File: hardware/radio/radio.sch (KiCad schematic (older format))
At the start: 4 parts, among them P101 CONN_01X04, P102 CONN_02X03, P103 CONN_02X05, P104 CONN_01X02

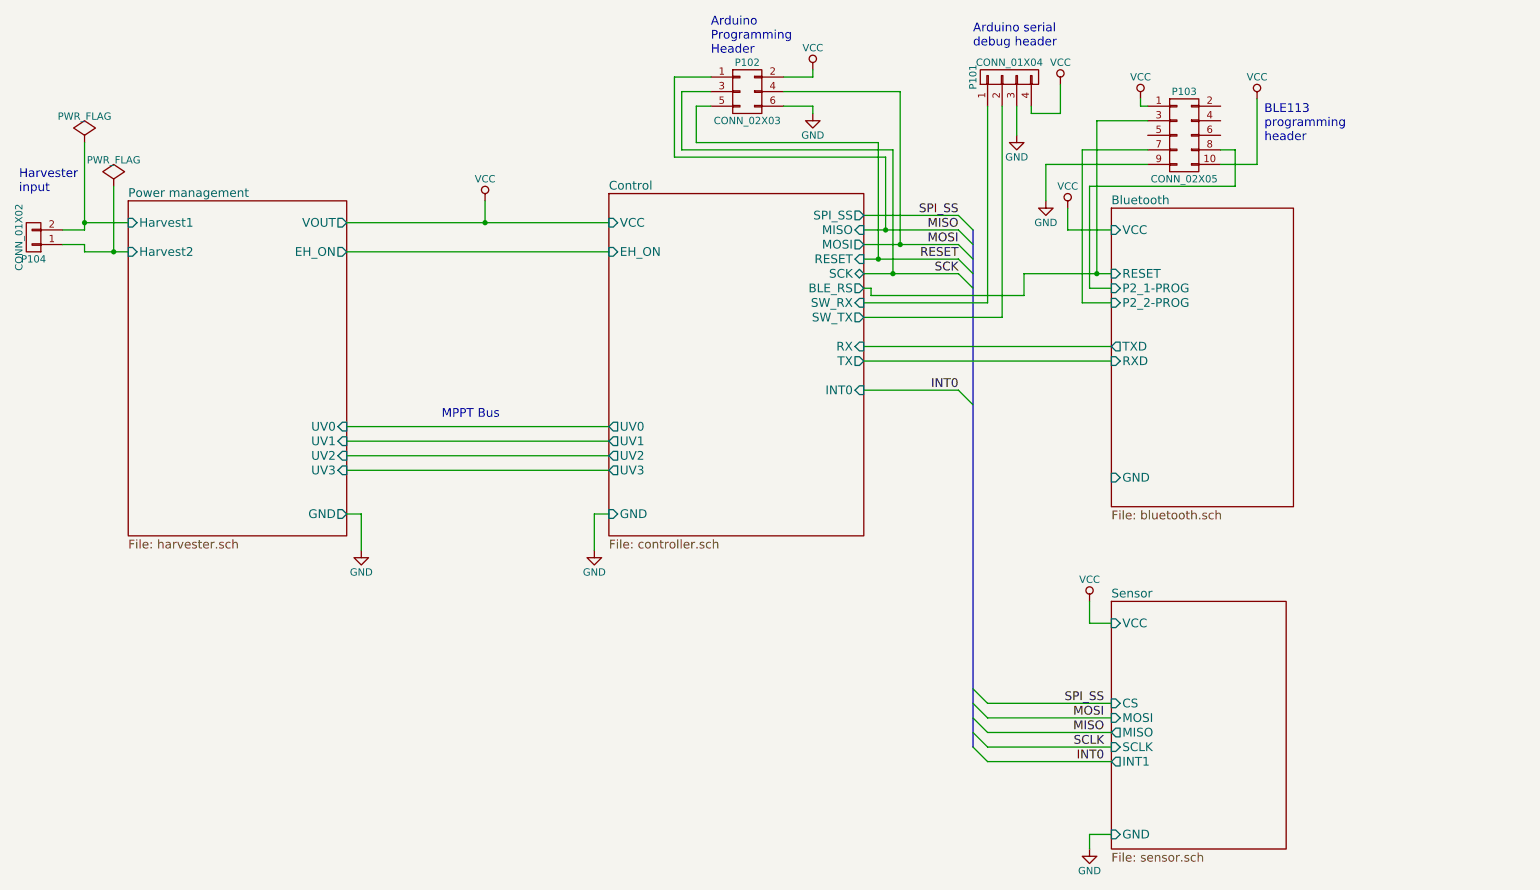
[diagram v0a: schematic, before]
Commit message: Add test points for current and voltage
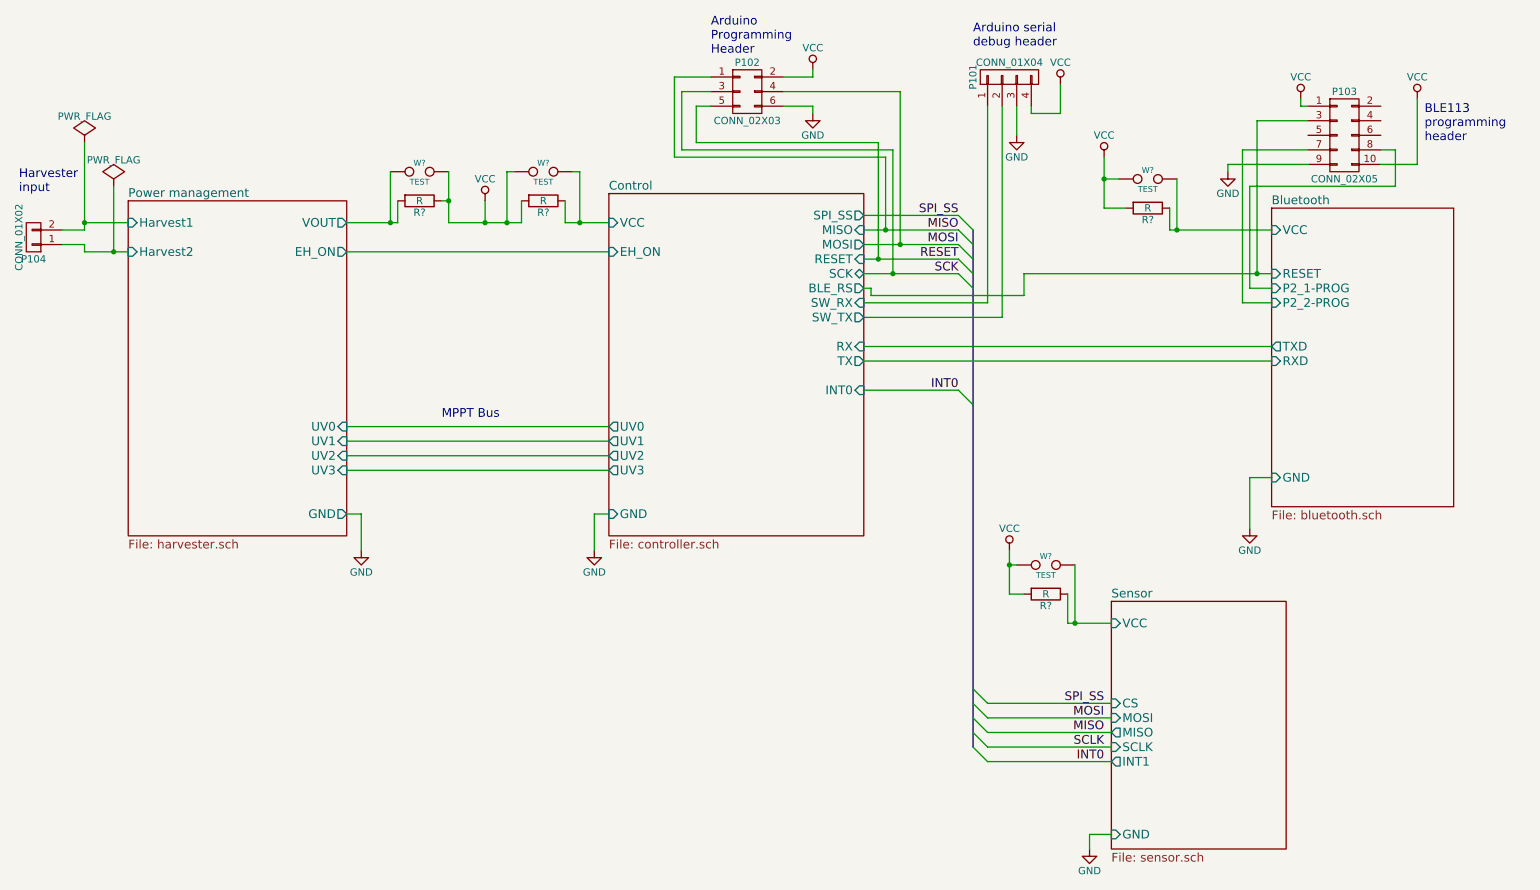
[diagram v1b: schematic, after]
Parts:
- added R? (x4): R, symbol R
- added W? (x4): TEST, symbol TEST
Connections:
- net VCC: now also R?.1, R?.2, R?.2, R?.2, W?.1, W?.1, W?.1, W?.2
- new net Bluetooth/VCC: R?.1, W?.2
- new net Control/VCC: R?.1, W?.2
- new net Power management/VOUT: R?.2, W?.1
- new net Sensor/VCC: R?.1, W?.2
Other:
- moved on the sheet: P103

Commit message: Assign testpoint footprints
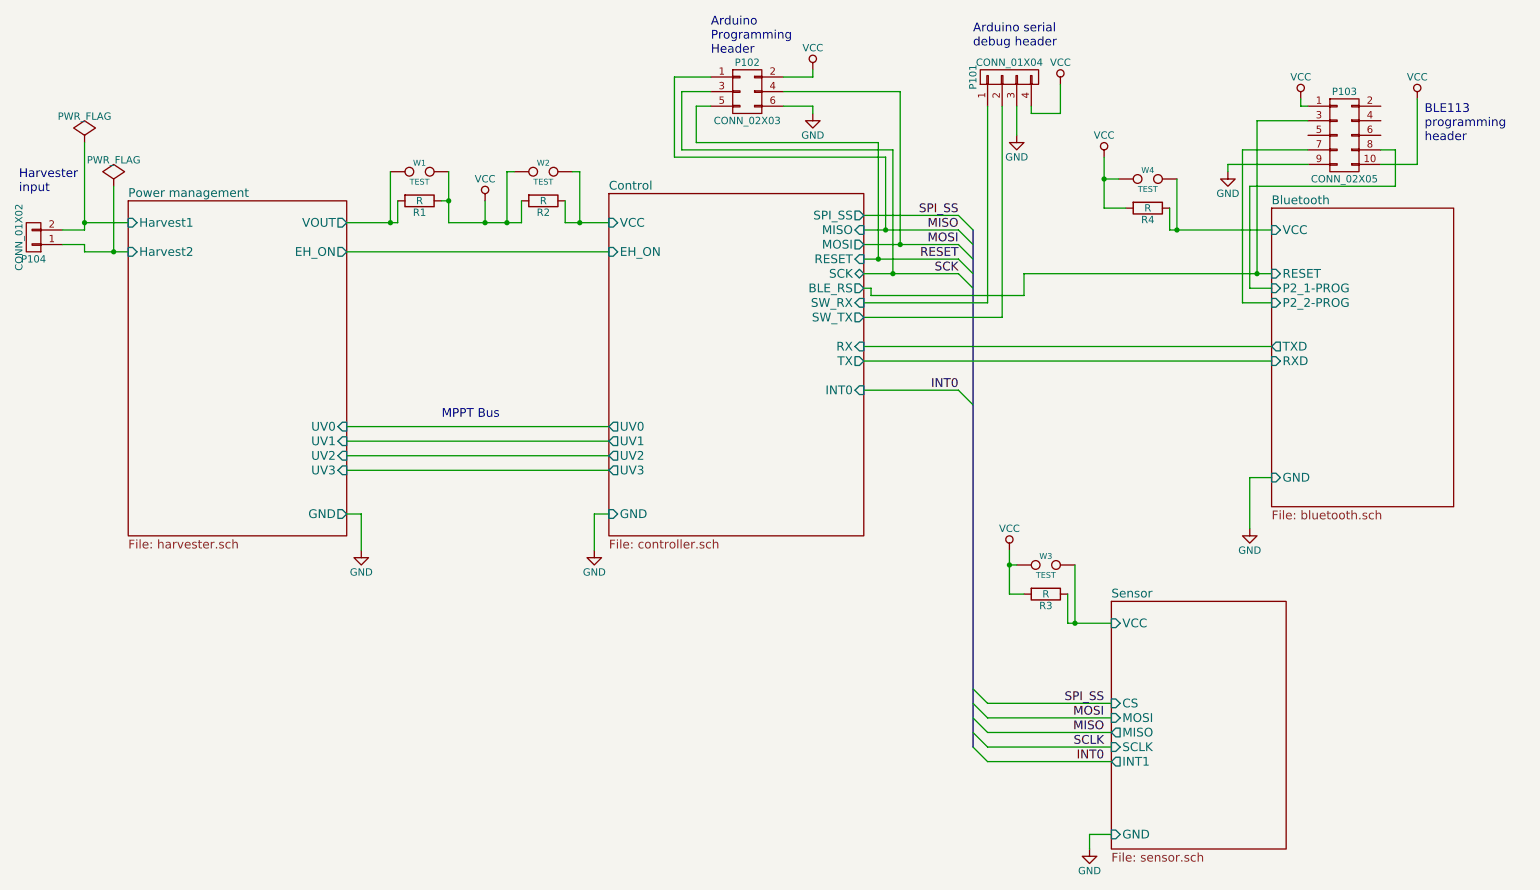
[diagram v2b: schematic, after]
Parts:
- P101: footprint (none) -> Pin_Headers:Pin_Header_Straight_1x04
- P102: footprint (none) -> Pin_Headers:Pin_Header_Straight_2x03
- P103: footprint (none) -> Pin_Headers:Pin_Header_Straight_2x05_Pitch1.27mm
- P104: footprint (none) -> Pin_Headers:Pin_Header_Straight_1x02
- R1, R2, R3, R4: renamed from R?; footprint (none) -> Resistors_SMD:R_0603
- W1, W2, W3, W4: renamed from W?; footprint (none) -> footprints_:Test_pair_TH_small
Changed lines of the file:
@@
 F 0 "P104" H 650 2200 50  0000 C CNN
 F 1 "CONN_01X02" V 750 2050 50  0000 C CNN
-F 2 "" H 650 2050 60  0000 C CNN
+F 2 "Pin_Headers:Pin_Header_Straight_1x02" H 650 2050 60  0001 C CNN
 F 3 "" H 650 2050 60  0000 C CNN
 	1    650  2050
@@
 F 0 "P103" H 9650 1650 50  0000 C CNN
 F 1 "CONN_02X05" H 9650 1050 50  0000 C CNN
-F 2 "" H 9650 150 60  0000 C CNN
+F 2 "Pin_Headers:Pin_Header_Straight_2x05_Pitch1.27mm" H 9650 150 60  0001 C CNN
 F 3 "" H 9650 150 60  0000 C CNN
 	1    9650 1350
@@
 BLE113\nprogramming\nheader
 $Comp
-L VCC #PWR09
+L VCC #PWR08
 U 1 1 55EC0D57
 P 3750 1800
-F 0 "#PWR09" H 3750 1650 50  0001 C CNN
+F 0 "#PWR08" H 3750 1650 50  0001 C CNN
 F 1 "VCC" H 3750 1950 50  0000 C CNN
 F 2 "" H 3750 1800 60  0000 C CNN
@@
 F 0 "P102" H 5550 1250 50  0000 C CNN
 F 1 "CONN_02X03" H 5550 850 50  0000 C CNN
-F 2 "" H 5550 -150 60  0000 C CNN
+F 2 "Pin_Headers:Pin_Header_Straight_2x03" H 5550 -150 60  0001 C CNN
 F 3 "" H 5550 -150 60  0000 C CNN
 	1    5550 1050
@@
 $EndComp
 $Comp
-L VCC #PWR010
+L VCC #PWR09
 U 1 1 55EC31B4
 P 6000 900
-F 0 "#PWR010" H 6000 750 50  0001 C CNN
+F 0 "#PWR09" H 6000 750 50  0001 C CNN
 F 1 "VCC" H 6000 1050 50  0000 C CNN
 F 2 "" H 6000 900 60  0000 C CNN
@@
 $EndComp
 $Comp
-L GND #PWR011
+L GND #PWR010
 U 1 1 55EC336C
 P 6000 1200
-F 0 "#PWR011" H 6000 950 50  0001 C CNN
+F 0 "#PWR010" H 6000 950 50  0001 C CNN
 F 1 "GND" H 6000 1050 50  0000 C CNN
 F 2 "" H 6000 1200 60  0000 C CNN
@@
 F 0 "P101" H 7350 1200 50  0000 C CNN
 F 1 "CONN_01X04" V 7450 950 50  0000 C CNN
-F 2 "" H 7350 950 60  0000 C CNN
+F 2 "Pin_Headers:Pin_Header_Straight_1x04" H 7350 950 60  0001 C CNN
 F 3 "" H 7350 950 60  0000 C CNN
 	1    7350 950
@@
 $EndComp
 $Comp
-L GND #PWR012
+L GND #PWR011
 U 1 1 55EC4334
 P 7400 1350
-F 0 "#PWR012" H 7400 1100 50  0001 C CNN
+F 0 "#PWR011" H 7400 1100 50  0001 C CNN
 F 1 "GND" H 7400 1200 50  0000 C CNN
 F 2 "" H 7400 1350 60  0000 C CNN
@@
 $EndComp
 $Comp
-L VCC #PWR013
+L VCC #PWR012
 U 1 1 55EC45C4
 P 7700 1000
-F 0 "#PWR013" H 7700 850 50  0001 C CNN
+F 0 "#PWR012" H 7700 850 50  0001 C CNN
 F 1 "VCC" H 7700 1150 50  0000 C CNN
 F 2 "" H 7700 1000 60  0000 C CNN
@@
 SPI_SS
 $Comp
-L GND #PWR014
+L GND #PWR013
 U 1 1 55ECE90B
 P 7900 6250
-F 0 "#PWR014" H 7900 6000 50  0001 C CNN
+F 0 "#PWR013" H 7900 6000 50  0001 C CNN
 F 1 "GND" H 7900 6100 50  0000 C CNN
 F 2 "" H 7900 6250 60  0000 C CNN
@@
 $EndComp
 $Comp
-L TEST W?
+L TEST W1
 U 1 1 55F2257E
 P 3300 1600
-F 0 "W?" H 3300 1660 40  0000 C CNN
+F 0 "W1" H 3300 1660 40  0000 C CNN
 F 1 "TEST" H 3300 1530 40  0000 C CNN
-F 2 "" H 3300 1600 60  0000 C CNN
+F 2 "footprints_:Test_pair_TH_small" H 3300 1600 60  0001 C CNN
 F 3 "" H 3300 1600 60  0000 C CNN
 	1    3300 1600
@@
 $EndComp
 $Comp
-L R R?
+L R R1
 U 1 1 55F23C0F
 P 3300 1800
-F 0 "R?" V 3380 1800 50  0000 C CNN
+F 0 "R1" V 3380 1800 50  0000 C CNN
 F 1 "R" V 3300 1800 50  0000 C CNN
-F 2 "" V 3230 1800 30  0000 C CNN
+F 2 "Resistors_SMD:R_0603" V 3230 1800 30  0001 C CNN
 F 3 "" H 3300 1800 30  0000 C CNN
 	1    3300 1800
@@
 $EndComp
 $Comp
-L TEST W?
+L TEST W2
 U 1 1 55F24693
 P 4150 1600
-F 0 "W?" H 4150 1660 40  0000 C CNN
+F 0 "W2" H 4150 1660 40  0000 C CNN
 F 1 "TEST" H 4150 1530 40  0000 C CNN
-F 2 "" H 4150 1600 60  0000 C CNN
+F 2 "footprints_:Test_pair_TH_small" H 4150 1600 60  0001 C CNN
 F 3 "" H 4150 1600 60  0000 C CNN
 	1    4150 1600
@@
 $EndComp
 $Comp
-L R R?
+L R R2
 U 1 1 55F24699
 P 4150 1800
-F 0 "R?" V 4230 1800 50  0000 C CNN
+F 0 "R2" V 4230 1800 50  0000 C CNN
 F 1 "R" V 4150 1800 50  0000 C CNN
-F 2 "" V 4080 1800 30  0000 C CNN
+F 2 "Resistors_SMD:R_0603" V 4080 1800 30  0001 C CNN
 F 3 "" H 4150 1800 30  0000 C CNN
 	1    4150 1800
@@
 $EndComp
 $Comp
-L TEST W?
+L TEST W3
 U 1 1 55F279B5
 P 7600 4300
-F 0 "W?" H 7600 4360 40  0000 C CNN
+F 0 "W3" H 7600 4360 40  0000 C CNN
 F 1 "TEST" H 7600 4230 40  0000 C CNN
-F 2 "" H 7600 4300 60  0000 C CNN
+F 2 "footprints_:Test_pair_TH_small" H 7600 4300 60  0001 C CNN
 F 3 "" H 7600 4300 60  0000 C CNN
 	1    7600 4300
@@
 $EndComp
 $Comp
-L R R?
+L R R3
 U 1 1 55F279BB
 P 7600 4500
-F 0 "R?" V 7680 4500 50  0000 C CNN
+F 0 "R3" V 7680 4500 50  0000 C CNN
 F 1 "R" V 7600 4500 50  0000 C CNN
-F 2 "" V 7530 4500 30  0000 C CNN
+F 2 "Resistors_SMD:R_0603" V 7530 4500 30  0001 C CNN
 F 3 "" H 7600 4500 30  0000 C CNN
 	1    7600 4500
@@
 $EndComp
 $Comp
-L TEST W?
+L TEST W4
 U 1 1 55F2AC1A
 P 8300 1650
-F 0 "W?" H 8300 1710 40  0000 C CNN
+F 0 "W4" H 8300 1710 40  0000 C CNN
 F 1 "TEST" H 8300 1580 40  0000 C CNN
-F 2 "" H 8300 1650 60  0000 C CNN
+F 2 "footprints_:Test_pair_TH_small" H 8300 1650 60  0001 C CNN
 F 3 "" H 8300 1650 60  0000 C CNN
 	1    8300 1650
@@
 $EndComp
 $Comp
-L R R?
+L R R4
 U 1 1 55F2AC20
 P 8300 1850
-F 0 "R?" V 8380 1850 50  0000 C CNN
+F 0 "R4" V 8380 1850 50  0000 C CNN
 F 1 "R" V 8300 1850 50  0000 C CNN
-F 2 "" V 8230 1850 30  0000 C CNN
+F 2 "Resistors_SMD:R_0603" V 8230 1850 30  0001 C CNN
 F 3 "" H 8300 1850 30  0000 C CNN
 	1    8300 1850
@@
 Connection ~ 8000 1650
 $Comp
-L VCC #PWR?
+L VCC #PWR014
 U 1 1 55F2CE55
 P 8000 1500
-F 0 "#PWR?" H 8000 1350 50  0001 C CNN
+F 0 "#PWR014" H 8000 1350 50  0001 C CNN
 F 1 "VCC" H 8000 1650 50  0000 C CNN
 F 2 "" H 8000 1500 60  0000 C CNN
@@
 Connection ~ 7350 4300
 $Comp
-L VCC #PWR?
+L VCC #PWR015
 U 1 1 55F30E46
 P 7350 4200
-F 0 "#PWR?" H 7350 4050 50  0001 C CNN
+F 0 "#PWR015" H 7350 4050 50  0001 C CNN
 F 1 "VCC" H 7350 4350 50  0000 C CNN
 F 2 "" H 7350 4200 60  0000 C CNN
@@
 	9000 3700 9000 4050
 $Comp
-L GND #PWR?
+L GND #PWR016
 U 1 1 55F3D092
 P 9000 4050
-F 0 "#PWR?" H 9000 3800 50  0001 C CNN
+F 0 "#PWR016" H 9000 3800 50  0001 C CNN
 F 1 "GND" H 9000 3900 50  0000 C CNN
 F 2 "" H 9000 4050 60  0000 C CNN

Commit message: Work on laying out TPs
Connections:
- net VCC: no longer P102.2 (P2), P103.1 (P1)
- net Bluetooth/VCC renamed VCC_BLE
- net VCC_BLE: now also P103.1 (P1)
- net Control/VCC renamed VCC_uc
- net VCC_uc: now also P102.2 (P2)
- net Power management/VOUT renamed VOUT
- net Sensor/VCC renamed VCC_ACC
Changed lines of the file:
@@
 F11 "INT0" I R 6350 3100 60
 F12 "GND" I L 4600 3950 60
-F13 "VCC" I L 4600 1950 60
+F13 "VCC_uc" I L 4600 1950 60
 F14 "UV0" O L 4600 3350 60
 F15 "UV1" O L 4600 3450 60
@@
 F3 "P2_1-PROG" I L 9150 2400 60
 F4 "P2_2-PROG" I L 9150 2500 60
-F5 "VCC" I L 9150 2000 60
+F5 "VCC_BLE" I L 9150 2000 60
 F6 "GND" I L 9150 3700 60
 F7 "TXD" O L 9150 2800 60
@@
 F5 "SCLK" I L 8050 5550 60
 F6 "INT1" O L 8050 5650 60
-F7 "VCC" I L 8050 4700 60
+F7 "VCC_ACC" I L 8050 4700 60
 F8 "GND" I L 8050 6150 60
 $EndSheet
@@
 $EndComp
 $Comp
-L VCC #PWR06
-U 1 1 55EBE126
-P 9350 1100
-F 0 "#PWR06" H 9350 950 50  0001 C CNN
-F 1 "VCC" H 9350 1250 50  0000 C CNN
-F 2 "" H 9350 1100 60  0000 C CNN
-F 3 "" H 9350 1100 60  0000 C CNN
-	1    9350 1100
-	1    0    0    -1
-$EndComp
-$Comp
-L GND #PWR07
+L GND #PWR06
 U 1 1 55EBE5B7
 P 8850 1600
-F 0 "#PWR07" H 8850 1350 50  0001 C CNN
+F 0 "#PWR06" H 8850 1350 50  0001 C CNN
 F 1 "GND" H 8850 1450 50  0000 C CNN
 F 2 "" H 8850 1600 60  0000 C CNN
@@
 BLE113\nprogramming\nheader
 $Comp
-L VCC #PWR08
+L VCC #PWR07
 U 1 1 55EC0D57
 P 3750 1800
-F 0 "#PWR08" H 3750 1650 50  0001 C CNN
+F 0 "#PWR07" H 3750 1650 50  0001 C CNN
 F 1 "VCC" H 3750 1950 50  0000 C CNN
 F 2 "" H 3750 1800 60  0000 C CNN
@@
 $EndComp
 $Comp
-L VCC #PWR09
-U 1 1 55EC31B4
-P 6000 900
-F 0 "#PWR09" H 6000 750 50  0001 C CNN
-F 1 "VCC" H 6000 1050 50  0000 C CNN
-F 2 "" H 6000 900 60  0000 C CNN
-F 3 "" H 6000 900 60  0000 C CNN
-	1    6000 900
-	1    0    0    -1
-$EndComp
-$Comp
-L GND #PWR010
+L GND #PWR08
 U 1 1 55EC336C
 P 6000 1200
-F 0 "#PWR010" H 6000 950 50  0001 C CNN
+F 0 "#PWR08" H 6000 950 50  0001 C CNN
 F 1 "GND" H 6000 1050 50  0000 C CNN
 F 2 "" H 6000 1200 60  0000 C CNN
@@
 $EndComp
 $Comp
-L GND #PWR011
+L GND #PWR09
 U 1 1 55EC4334
 P 7400 1350
-F 0 "#PWR011" H 7400 1100 50  0001 C CNN
+F 0 "#PWR09" H 7400 1100 50  0001 C CNN
 F 1 "GND" H 7400 1200 50  0000 C CNN
 F 2 "" H 7400 1350 60  0000 C CNN
@@
 $EndComp
 $Comp
-L VCC #PWR012
+L VCC #PWR010
 U 1 1 55EC45C4
 P 7700 1000
-F 0 "#PWR012" H 7700 850 50  0001 C CNN
+F 0 "#PWR010" H 7700 850 50  0001 C CNN
 F 1 "VCC" H 7700 1150 50  0000 C CNN
 F 2 "" H 7700 1000 60  0000 C CNN
@@
 SPI_SS
 $Comp
-L GND #PWR013
+L GND #PWR011
 U 1 1 55ECE90B
 P 7900 6250
-F 0 "#PWR013" H 7900 6000 50  0001 C CNN
+F 0 "#PWR011" H 7900 6000 50  0001 C CNN
 F 1 "GND" H 7900 6100 50  0000 C CNN
 F 2 "" H 7900 6250 60  0000 C CNN
@@
 Connection ~ 8000 1650
 $Comp
-L VCC #PWR014
+L VCC #PWR012
 U 1 1 55F2CE55
 P 8000 1500
-F 0 "#PWR014" H 8000 1350 50  0001 C CNN
+F 0 "#PWR012" H 8000 1350 50  0001 C CNN
 F 1 "VCC" H 8000 1650 50  0000 C CNN
 F 2 "" H 8000 1500 60  0000 C CNN
@@
 Connection ~ 7350 4300
 $Comp
-L VCC #PWR015
+L VCC #PWR013
 U 1 1 55F30E46
 P 7350 4200
-F 0 "#PWR015" H 7350 4050 50  0001 C CNN
+F 0 "#PWR013" H 7350 4050 50  0001 C CNN
 F 1 "VCC" H 7350 4350 50  0000 C CNN
 F 2 "" H 7350 4200 60  0000 C CNN
@@
 	9000 3700 9000 4050
 $Comp
-L GND #PWR016
+L GND #PWR014
 U 1 1 55F3D092
 P 9000 4050
-F 0 "#PWR016" H 9000 3800 50  0001 C CNN
+F 0 "#PWR014" H 9000 3800 50  0001 C CNN
 F 1 "GND" H 9000 3900 50  0000 C CNN
 F 2 "" H 9000 4050 60  0000 C CNN
@@
 	1    0    0    -1
 $EndComp
+Text Label 3100 1600 2    60   ~ 0
+VOUT
+Text Label 4400 1600 0    60   ~ 0
+VCC_uc
+Text Label 6000 900  0    60   ~ 0
+VCC_uc
+Text Label 8900 2000 2    60   ~ 0
+VCC_BLE
+Text Label 9350 1100 2    60   ~ 0
+VCC_BLE
+Text Label 7800 4400 0    60   ~ 0
+VCC_ACC
 $EndSCHEMATC

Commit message: Parts placed
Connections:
- net VCC: no longer P101.4 (P4)
- net VCC_uc: now also P101.4 (P4)
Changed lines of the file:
@@
-	1    0    0    -1
-$EndComp
-$Comp
-L VCC #PWR010
-U 1 1 55EC45C4
-P 7700 1000
-F 0 "#PWR010" H 7700 850 50  0001 C CNN
-F 1 "VCC" H 7700 1150 50  0000 C CNN
-F 2 "" H 7700 1000 60  0000 C CNN
-F 3 "" H 7700 1000 60  0000 C CNN
-	1    7700 1000
 	1    0    0    -1
 $EndComp
@@
 SPI_SS
 $Comp
-L GND #PWR011
+L GND #PWR010
 U 1 1 55ECE90B
 P 7900 6250
-F 0 "#PWR011" H 7900 6000 50  0001 C CNN
+F 0 "#PWR010" H 7900 6000 50  0001 C CNN
 F 1 "GND" H 7900 6100 50  0000 C CNN
 F 2 "" H 7900 6250 60  0000 C CNN
@@
 Connection ~ 8000 1650
 $Comp
-L VCC #PWR012
+L VCC #PWR011
 U 1 1 55F2CE55
 P 8000 1500
-F 0 "#PWR012" H 8000 1350 50  0001 C CNN
+F 0 "#PWR011" H 8000 1350 50  0001 C CNN
 F 1 "VCC" H 8000 1650 50  0000 C CNN
 F 2 "" H 8000 1500 60  0000 C CNN
@@
 Connection ~ 7350 4300
 $Comp
-L VCC #PWR013
+L VCC #PWR012
 U 1 1 55F30E46
 P 7350 4200
-F 0 "#PWR013" H 7350 4050 50  0001 C CNN
+F 0 "#PWR012" H 7350 4050 50  0001 C CNN
 F 1 "VCC" H 7350 4350 50  0000 C CNN
 F 2 "" H 7350 4200 60  0000 C CNN
@@
 	9000 3700 9000 4050
 $Comp
-L GND #PWR014
+L GND #PWR013
 U 1 1 55F3D092
 P 9000 4050
-F 0 "#PWR014" H 9000 3800 50  0001 C CNN
+F 0 "#PWR013" H 9000 3800 50  0001 C CNN
 F 1 "GND" H 9000 3900 50  0000 C CNN
 F 2 "" H 9000 4050 60  0000 C CNN
@@
 Text Label 7800 4400 0    60   ~ 0
 VCC_ACC
+Text Label 7700 1000 0    60   ~ 0
+VCC_uc
 $EndSCHEMATC

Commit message: Routing finalized
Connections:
- net VCC: no longer P103.10 (P10)
- net VCC_BLE: now also P103.10 (P10)
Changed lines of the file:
@@
 F3 "MOSI" I L 8050 5350 60
 F4 "MISO" O L 8050 5450 60
-F5 "SCLK" I L 8050 5550 60
+F5 "SCL" I L 8050 5550 60
 F6 "INT1" O L 8050 5650 60
 F7 "VCC_ACC" I L 8050 4700 60
@@
 $EndComp
 $Comp
-L VCC #PWR05
-U 1 1 55EBE042
-P 10150 1100
-F 0 "#PWR05" H 10150 950 50  0001 C CNN
-F 1 "VCC" H 10150 1250 50  0000 C CNN
-F 2 "" H 10150 1100 60  0000 C CNN
-F 3 "" H 10150 1100 60  0000 C CNN
-	1    10150 1100
-	1    0    0    -1
-$EndComp
-$Comp
-L GND #PWR06
+L GND #PWR05
 U 1 1 55EBE5B7
 P 8850 1600
-F 0 "#PWR06" H 8850 1350 50  0001 C CNN
+F 0 "#PWR05" H 8850 1350 50  0001 C CNN
 F 1 "GND" H 8850 1450 50  0000 C CNN
 F 2 "" H 8850 1600 60  0000 C CNN
@@
 BLE113\nprogramming\nheader
 $Comp
-L VCC #PWR07
+L VCC #PWR06
 U 1 1 55EC0D57
 P 3750 1800
-F 0 "#PWR07" H 3750 1650 50  0001 C CNN
+F 0 "#PWR06" H 3750 1650 50  0001 C CNN
 F 1 "VCC" H 3750 1950 50  0000 C CNN
 F 2 "" H 3750 1800 60  0000 C CNN
@@
 $EndComp
 $Comp
-L GND #PWR08
+L GND #PWR07
 U 1 1 55EC336C
 P 6000 1200
-F 0 "#PWR08" H 6000 950 50  0001 C CNN
+F 0 "#PWR07" H 6000 950 50  0001 C CNN
 F 1 "GND" H 6000 1050 50  0000 C CNN
 F 2 "" H 6000 1200 60  0000 C CNN
@@
 $EndComp
 $Comp
-L GND #PWR09
+L GND #PWR08
 U 1 1 55EC4334
 P 7400 1350
-F 0 "#PWR09" H 7400 1100 50  0001 C CNN
+F 0 "#PWR08" H 7400 1100 50  0001 C CNN
 F 1 "GND" H 7400 1200 50  0000 C CNN
 F 2 "" H 7400 1350 60  0000 C CNN
@@
 INT0
 Text Label 8000 5550 2    60   ~ 0
-SCLK
+SCK
 Text Label 8000 5450 2    60   ~ 0
 MISO
@@
 SPI_SS
 $Comp
-L GND #PWR010
+L GND #PWR09
 U 1 1 55ECE90B
 P 7900 6250
-F 0 "#PWR010" H 7900 6000 50  0001 C CNN
+F 0 "#PWR09" H 7900 6000 50  0001 C CNN
 F 1 "GND" H 7900 6100 50  0000 C CNN
 F 2 "" H 7900 6250 60  0000 C CNN
@@
 Connection ~ 8000 1650
 $Comp
-L VCC #PWR011
+L VCC #PWR010
 U 1 1 55F2CE55
 P 8000 1500
-F 0 "#PWR011" H 8000 1350 50  0001 C CNN
+F 0 "#PWR010" H 8000 1350 50  0001 C CNN
 F 1 "VCC" H 8000 1650 50  0000 C CNN
 F 2 "" H 8000 1500 60  0000 C CNN
@@
 Connection ~ 7350 4300
 $Comp
-L VCC #PWR012
+L VCC #PWR011
 U 1 1 55F30E46
 P 7350 4200
-F 0 "#PWR012" H 7350 4050 50  0001 C CNN
+F 0 "#PWR011" H 7350 4050 50  0001 C CNN
 F 1 "VCC" H 7350 4350 50  0000 C CNN
 F 2 "" H 7350 4200 60  0000 C CNN
@@
 	9000 3700 9000 4050
 $Comp
-L GND #PWR013
+L GND #PWR012
 U 1 1 55F3D092
 P 9000 4050
-F 0 "#PWR013" H 9000 3800 50  0001 C CNN
+F 0 "#PWR012" H 9000 3800 50  0001 C CNN
 F 1 "GND" H 9000 3900 50  0000 C CNN
 F 2 "" H 9000 4050 60  0000 C CNN
@@
 Text Label 7700 1000 0    60   ~ 0
 VCC_uc
+Text Label 10150 1100 0    60   ~ 0
+VCC_BLE
 $EndSCHEMATC
